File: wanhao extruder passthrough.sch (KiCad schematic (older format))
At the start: 8 parts, among them J1 Conn_02x10_Counter_Clockwise, T0 Conn_01x02

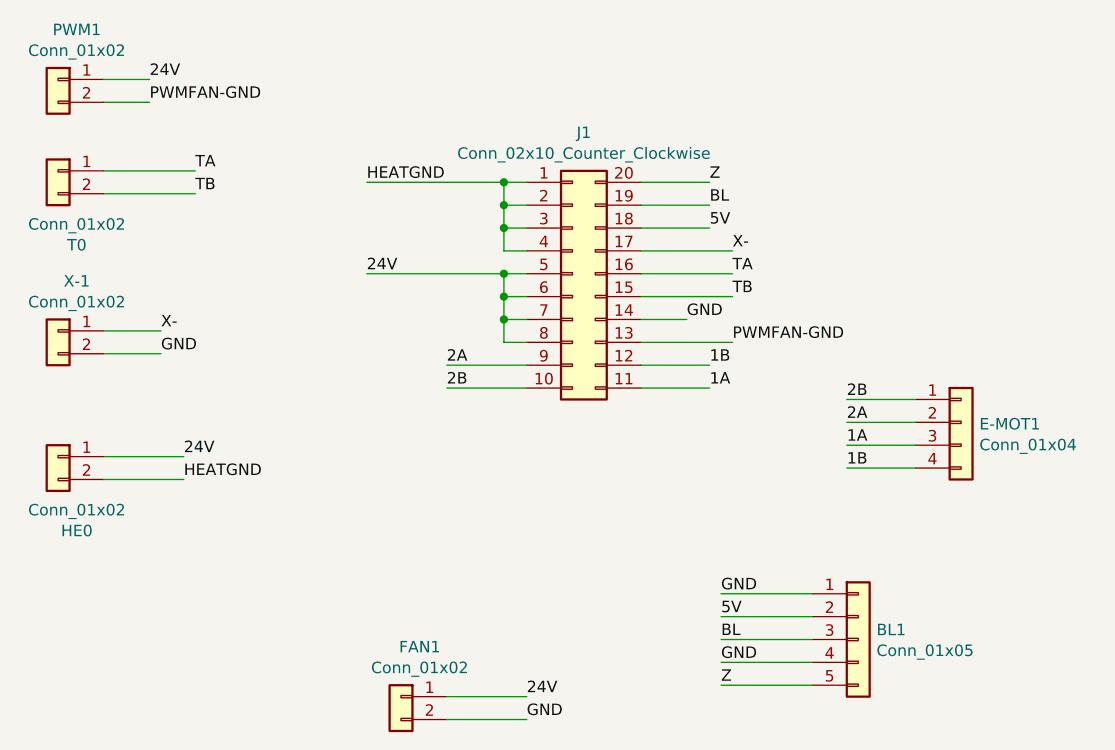
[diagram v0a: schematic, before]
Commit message: Added extender
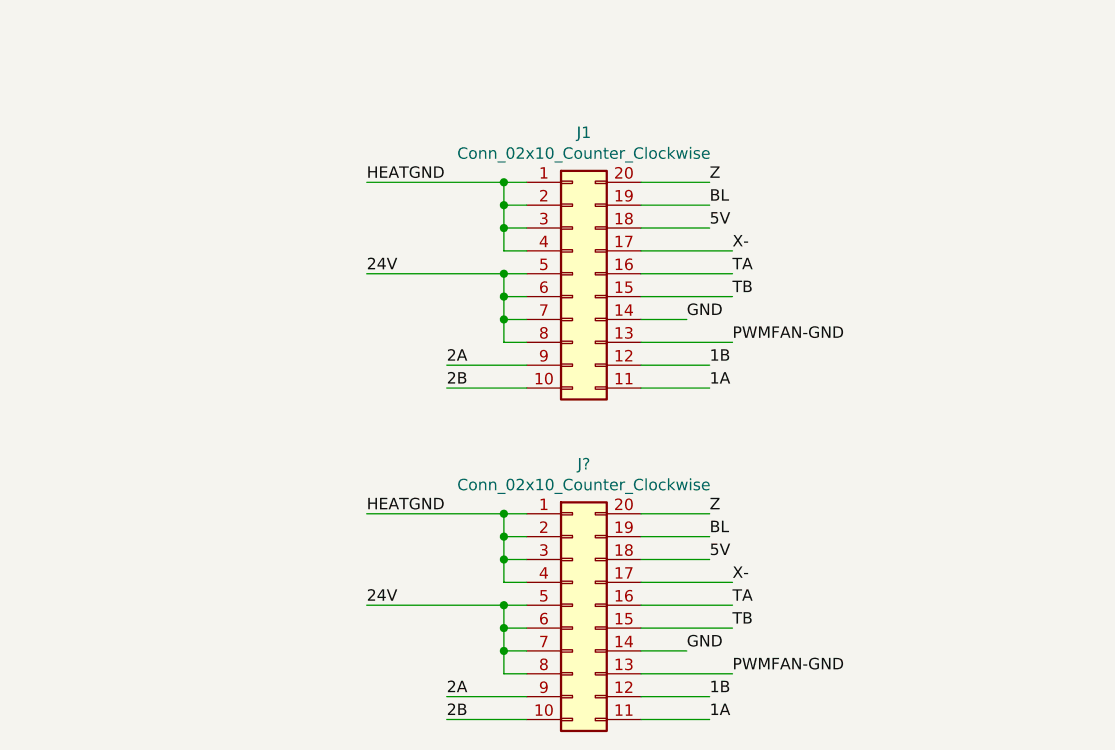
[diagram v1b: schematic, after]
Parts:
- removed BL1: Conn_01x05, Project:B5B-ZR, symbol Connector_Generic:Conn_01x05
- removed E-MOT1: Conn_01x04, Connector_JST:JST_XH_B4B-XH-A_1x04_P2.50mm_Vertical, symbol Connector_Generic:Conn_01x04
- removed FAN1, HE0, PWM1, T0, X-1: Conn_01x02, Connector_JST:JST_XH_B2B-XH-A_1x02_P2.50mm_Vertical, symbol Connector_Generic:Conn_01x02
- added J?: Conn_02x10_Counter_Clockwise, Connector_IDC:IDC-Header_2x10_P2.54mm_Vertical_Lock, symbol Connector_Generic:Conn_02x10_Counter_Clockwise
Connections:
- net 1A: now also J?.11 (Pin_11)
- net 1B: now also J?.12 (Pin_12)
- net 24V: now also J?.5 (Pin_5), J?.6 (Pin_6), J?.7 (Pin_7), J?.8 (Pin_8)
- net 2A: now also J?.9 (Pin_9)
- net 2B: now also J?.10 (Pin_10)
- net 5V: now also J?.18 (Pin_18)
- net BL: now also J?.19 (Pin_19)
- net GND: now also J?.14 (Pin_14)
- net HEATGND: now also J?.1 (Pin_1), J?.2 (Pin_2), J?.3 (Pin_3), J?.4 (Pin_4)
- net PWMFAN-GND: now also J?.13 (Pin_13)
- net TA: now also J?.16 (Pin_16)
- net TB: now also J?.15 (Pin_15)
- net X-: now also J?.17 (Pin_17)
- net Z: now also J?.20 (Pin_20)
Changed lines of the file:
@@
 EESchema Schematic File Version 4
-LIBS:wanhao extruder pcb-cache
 EELAYER 30 0
 EELAYER END
@@
 $EndDescr
 $Comp
-L Connector_Generic:Conn_01x02 PWM1
-U 1 1 5D7410E9
-P 2950 1800
-F 0 "PWM1" H 2868 2017 50  0000 C CNN
-F 1 "Conn_01x02" H 2868 1926 50  0000 C CNN
-F 2 "Connector_JST:JST_XH_B2B-XH-A_1x02_P2.50mm_Vertical" H 2950 1800 50  0001 C CNN
-F 3 "~" H 2950 1800 50  0001 C CNN
-	1    2950 1800
-	-1   0    0    -1
-$EndComp
-$Comp
-L Connector_Generic:Conn_01x02 T0
-U 1 1 5D74227E
-P 2950 2200
-F 0 "T0" H 2868 1875 50  0000 C CNN
-F 1 "Conn_01x02" H 2868 1966 50  0000 C CNN
-F 2 "Connector_JST:JST_XH_B2B-XH-A_1x02_P2.50mm_Vertical" H 2950 2200 50  0001 C CNN
-F 3 "~" H 2950 2200 50  0001 C CNN
-	1    2950 2200
-	-1   0    0    -1
-$EndComp
-$Comp
-L Connector_Generic:Conn_01x02 HE0
-U 1 1 5D74344F
-P 2950 3450
-F 0 "HE0" H 2868 3125 50  0000 C CNN
-F 1 "Conn_01x02" H 2868 3216 50  0000 C CNN
-F 2 "Connector_JST:JST_XH_B2B-XH-A_1x02_P2.50mm_Vertical" H 2950 3450 50  0001 C CNN
-F 3 "~" H 2950 3450 50  0001 C CNN
-	1    2950 3450
-	-1   0    0    -1
-$EndComp
-$Comp
-L Connector_Generic:Conn_01x02 FAN1
-U 1 1 5D743AA1
-P 4450 4500
-F 0 "FAN1" H 4368 4717 50  0000 C CNN
-F 1 "Conn_01x02" H 4368 4626 50  0000 C CNN
-F 2 "Connector_JST:JST_XH_B2B-XH-A_1x02_P2.50mm_Vertical" H 4450 4500 50  0001 C CNN
-F 3 "~" H 4450 4500 50  0001 C CNN
-	1    4450 4500
-	-1   0    0    -1
-$EndComp
-$Comp
 L Connector_Generic:Conn_02x10_Counter_Clockwise J1
 U 1 1 5D73EC2A
@@
 	1    0    0    -1
 $EndComp
-$Comp
-L Connector_Generic:Conn_01x02 X-1
-U 1 1 5D742D3A
-P 2950 2900
-F 0 "X-1" H 2868 3117 50  0000 C CNN
-F 1 "Conn_01x02" H 2868 3026 50  0000 C CNN
-F 2 "Connector_JST:JST_XH_B2B-XH-A_1x02_P2.50mm_Vertical" H 2950 2900 50  0001 C CNN
-F 3 "~" H 2950 2900 50  0001 C CNN
-	1    2950 2900
-	-1   0    0    -1
-$EndComp
 Text Label 4300 2250 0    50   ~ 0
 HEATGND
@@
 Wire Wire Line
 	5900 2950 5500 2950
-Text Label 3350 1900 0    50   ~ 0
-PWMFAN-GND
-Wire Wire Line
-	3350 1900 3150 1900
-Text Label 3350 1800 0    50   ~ 0
-24V
-Wire Wire Line
-	3350 1800 3150 1800
 Text Label 5900 2750 0    50   ~ 0
 TB
@@
 Wire Wire Line
 	5500 2650 5900 2650
-Wire Wire Line
-	3150 2200 3550 2200
-Text Label 3550 2200 0    50   ~ 0
-TA
-Wire Wire Line
-	3550 2300 3150 2300
-Text Label 3550 2300 0    50   ~ 0
-TB
 Text Label 5900 2550 0    50   ~ 0
 X-
-Text Label 3400 2900 0    50   ~ 0
-X-
-Text Label 3400 3000 0    50   ~ 0
-GND
-Wire Wire Line
-	3400 3000 3150 3000
-Wire Wire Line
-	3400 2900 3150 2900
-$Comp
-L Connector_Generic:Conn_01x05 BL1
-U 1 1 5D759D14
-P 6450 4250
-F 0 "BL1" H 6530 4292 50  0000 L CNN
-F 1 "Conn_01x05" H 6530 4201 50  0000 L CNN
-F 2 "Project:B5B-ZR" H 6450 4250 50  0001 C CNN
-F 3 "~" H 6450 4250 50  0001 C CNN
-	1    6450 4250
-	1    0    0    -1
-$EndComp
-$Comp
-L Connector_Generic:Conn_01x04 E-MOT1
-U 1 1 5D75A424
-P 6900 3300
-F 0 "E-MOT1" H 6980 3292 50  0000 L CNN
-F 1 "Conn_01x04" H 6980 3201 50  0000 L CNN
-F 2 "Connector_JST:JST_XH_B4B-XH-A_1x04_P2.50mm_Vertical" H 6900 3300 50  0001 C CNN
-F 3 "~" H 6900 3300 50  0001 C CNN
-	1    6900 3300
-	1    0    0    -1
-$EndComp
 Text Label 4650 3050 0    50   ~ 0
 2A
@@
 Wire Wire Line
 	5500 2850 5700 2850
-Text Label 6400 3200 0    50   ~ 0
-2B
-Text Label 6400 3300 0    50   ~ 0
-2A
-Text Label 6400 3400 0    50   ~ 0
-1A
-Text Label 6400 3500 0    50   ~ 0
-1B
-Wire Wire Line
-	6400 3200 6700 3200
-Wire Wire Line
-	6400 3300 6700 3300
-Wire Wire Line
-	6400 3400 6700 3400
-Wire Wire Line
-	6400 3500 6700 3500
-Text Label 5850 4050 0    50   ~ 0
-GND
-Text Label 5850 4150 0    50   ~ 0
-5V
-Text Label 5850 4250 0    50   ~ 0
-BL
-Text Label 5850 4350 0    50   ~ 0
-GND
-Text Label 5850 4450 0    50   ~ 0
-Z
-Wire Wire Line
-	5850 4050 6250 4050
-Wire Wire Line
-	5850 4150 6250 4150
-Wire Wire Line
-	5850 4250 6250 4250
-Wire Wire Line
-	5850 4350 6250 4350
-Wire Wire Line
-	5850 4450 6250 4450
 Text Label 5800 2250 0    50   ~ 0
 Z
@@
 Wire Wire Line
 	5800 2250 5500 2250
-Text Label 3500 3450 0    50   ~ 0
+$Comp
+L Connector_Generic:Conn_02x10_Counter_Clockwise J?
+U 1 1 5D76E5A0
+P 5200 4100
+F 0 "J?" H 5250 4717 50  0000 C CNN
+F 1 "Conn_02x10_Counter_Clockwise" H 5250 4626 50  0000 C CNN
+F 2 "Connector_IDC:IDC-Header_2x10_P2.54mm_Vertical_Lock" H 5200 4100 50  0001 C CNN
+F 3 "~" H 5200 4100 50  0001 C CNN
+	1    5200 4100
+	1    0    0    -1
+$EndComp
+Text Label 4300 3700 0    50   ~ 0
+HEATGND
+Wire Wire Line
+	4300 3700 4900 3700
+Wire Wire Line
+	5000 3800 4900 3800
+Wire Wire Line
+	4900 3800 4900 3700
+Connection ~ 4900 3700
+Wire Wire Line
+	4900 3700 5000 3700
+Wire Wire Line
+	5000 3900 4900 3900
+Wire Wire Line
+	4900 3900 4900 3800
+Connection ~ 4900 3800
+Wire Wire Line
+	5000 4000 4900 4000
+Wire Wire Line
+	4900 4000 4900 3900
+Connection ~ 4900 3900
+Text Label 4300 4100 0    50   ~ 0
 24V
-Text Label 3500 3550 0    50   ~ 0
-HEATGND
-Wire Wire Line
-	3150 3450 3500 3450
-Wire Wire Line
-	3150 3550 3500 3550
-Text Label 5000 4500 0    50   ~ 0
-24V
-Text Label 5000 4600 0    50   ~ 0
+Wire Wire Line
+	4300 4100 4900 4100
+Wire Wire Line
+	5000 4200 4900 4200
+Wire Wire Line
+	4900 4200 4900 4100
+Connection ~ 4900 4100
+Wire Wire Line
+	4900 4100 5000 4100
+Wire Wire Line
+	5000 4300 4900 4300
+Wire Wire Line
+	4900 4300 4900 4200
+Connection ~ 4900 4200
+Wire Wire Line
+	5000 4400 4900 4400
+Wire Wire Line
+	4900 4400 4900 4300
+Connection ~ 4900 4300
+Text Label 5900 4400 0    50   ~ 0
+PWMFAN-GND
+Wire Wire Line
+	5900 4400 5500 4400
+Text Label 5900 4200 0    50   ~ 0
+TB
+Text Label 5900 4100 0    50   ~ 0
+TA
+Wire Wire Line
+	5500 4100 5900 4100
+Text Label 5900 4000 0    50   ~ 0
+X-
+Text Label 4650 4500 0    50   ~ 0
+2A
+Text Label 4650 4600 0    50   ~ 0
+2B
+Text Label 5800 4600 0    50   ~ 0
+1A
+Text Label 5800 4500 0    50   ~ 0
+1B
+Wire Wire Line
+	5900 4200 5500 4200
+Wire Wire Line
+	5500 4500 5800 4500
+Wire Wire Line
+	5500 4600 5800 4600
+Wire Wire Line
+	5000 4500 4650 4500
+Wire Wire Line
+	5000 4600 4650 4600
+Wire Wire Line
+	5500 4000 5900 4000
+Text Label 5700 4300 0    50   ~ 0
 GND
 Wire Wire Line
-	4650 4500 5000 4500
-Wire Wire Line
-	5000 4600 4650 4600
+	5500 4300 5700 4300
+Text Label 5800 3700 0    50   ~ 0
+Z
+Text Label 5800 3800 0    50   ~ 0
+BL
+Text Label 5800 3900 0    50   ~ 0
+5V
+Wire Wire Line
+	5800 3900 5500 3900
+Wire Wire Line
+	5500 3800 5800 3800
+Wire Wire Line
+	5800 3700 5500 3700
 $EndSCHEMATC
